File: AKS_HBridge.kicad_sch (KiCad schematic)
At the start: 0 parts

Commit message: schematic brainstorming
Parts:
- added U1: DRV8262DDVR, DDV0044E-IPC_A, symbol custom_components:DRV8262DDVR

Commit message: linux wtf
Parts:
- added C1: 1uF, Capacitor_SMD:C_0603_1608Metric, symbol Device:C_Small
- added NT1: STARGND, symbol Device:NetTie_2
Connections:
- net GND: now also U1.10 (PGND34), U1.13 (PGND12), U1.20 (PGND12), U1.3 (PGND34), NT1.1
- net GNDS: now reaches U1.1 (GND)
- net GNDS: now also U1.44 (GND), NT1.2
- net VBUS: now reaches U1.11 (VM)
- net VBUS: now also U1.12 (VM), U1.2 (VM), U1.21 (VM), C1.1
- net MOT_B: now reaches U1.14 (OUT2)
- net MOT_B: now also U1.15 (OUT2), U1.16 (OUT2), U1.7 (OUT4), U1.8 (OUT4), U1.9 (OUT4)
- net MOT_A: now reaches U1.17 (OUT1)
- net MOT_A: now also U1.18 (OUT1), U1.19 (OUT1), U1.4 (OUT3), U1.5 (OUT3), U1.6 (OUT3)
- net at U1.22 (VCP): now also C1.2
- net VCC: now reaches U1.42 (VCC)
- net VCC: now also U1.43 (DVDD)
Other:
- company: (none) -> iRobotics
- title: (none) -> AKS Brake Actuator H-Bridge
- moved on the sheet: U1

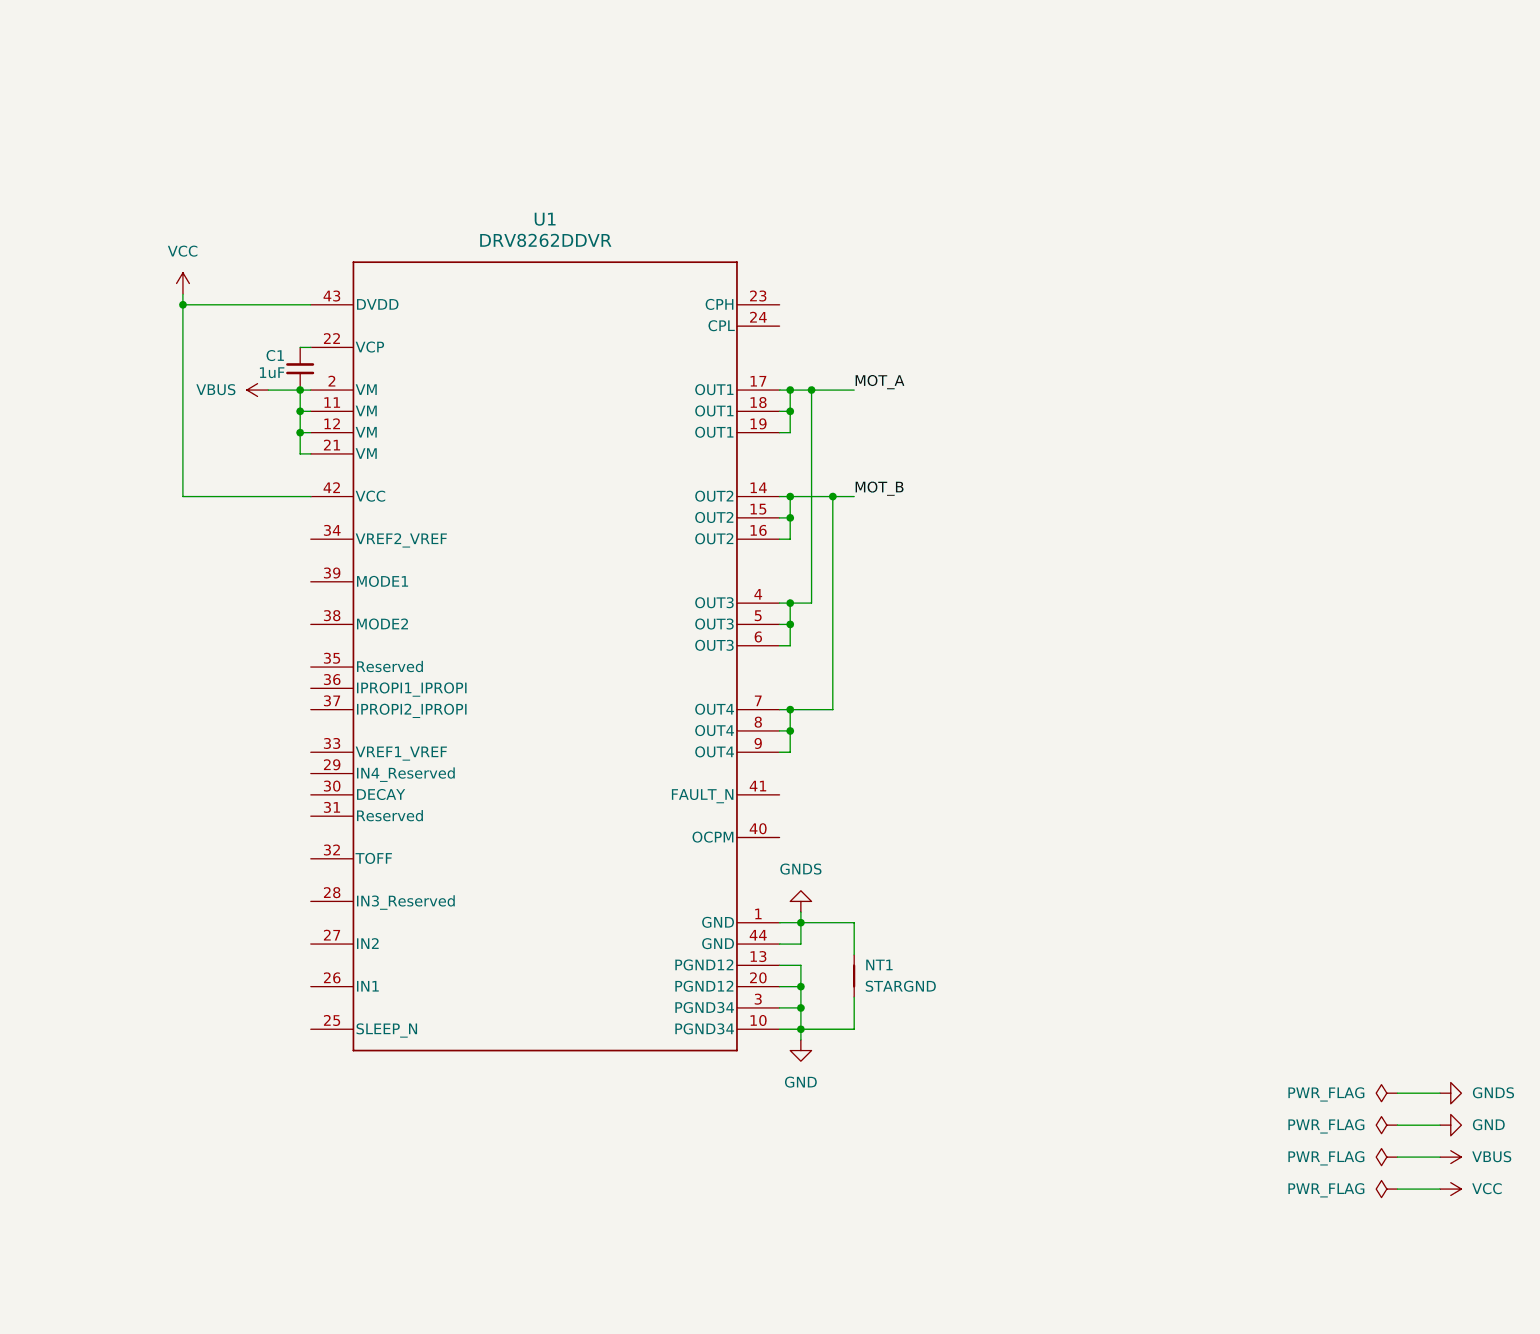
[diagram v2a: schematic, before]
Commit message: schematic done with exception of control connector socket type, probably JST-PH
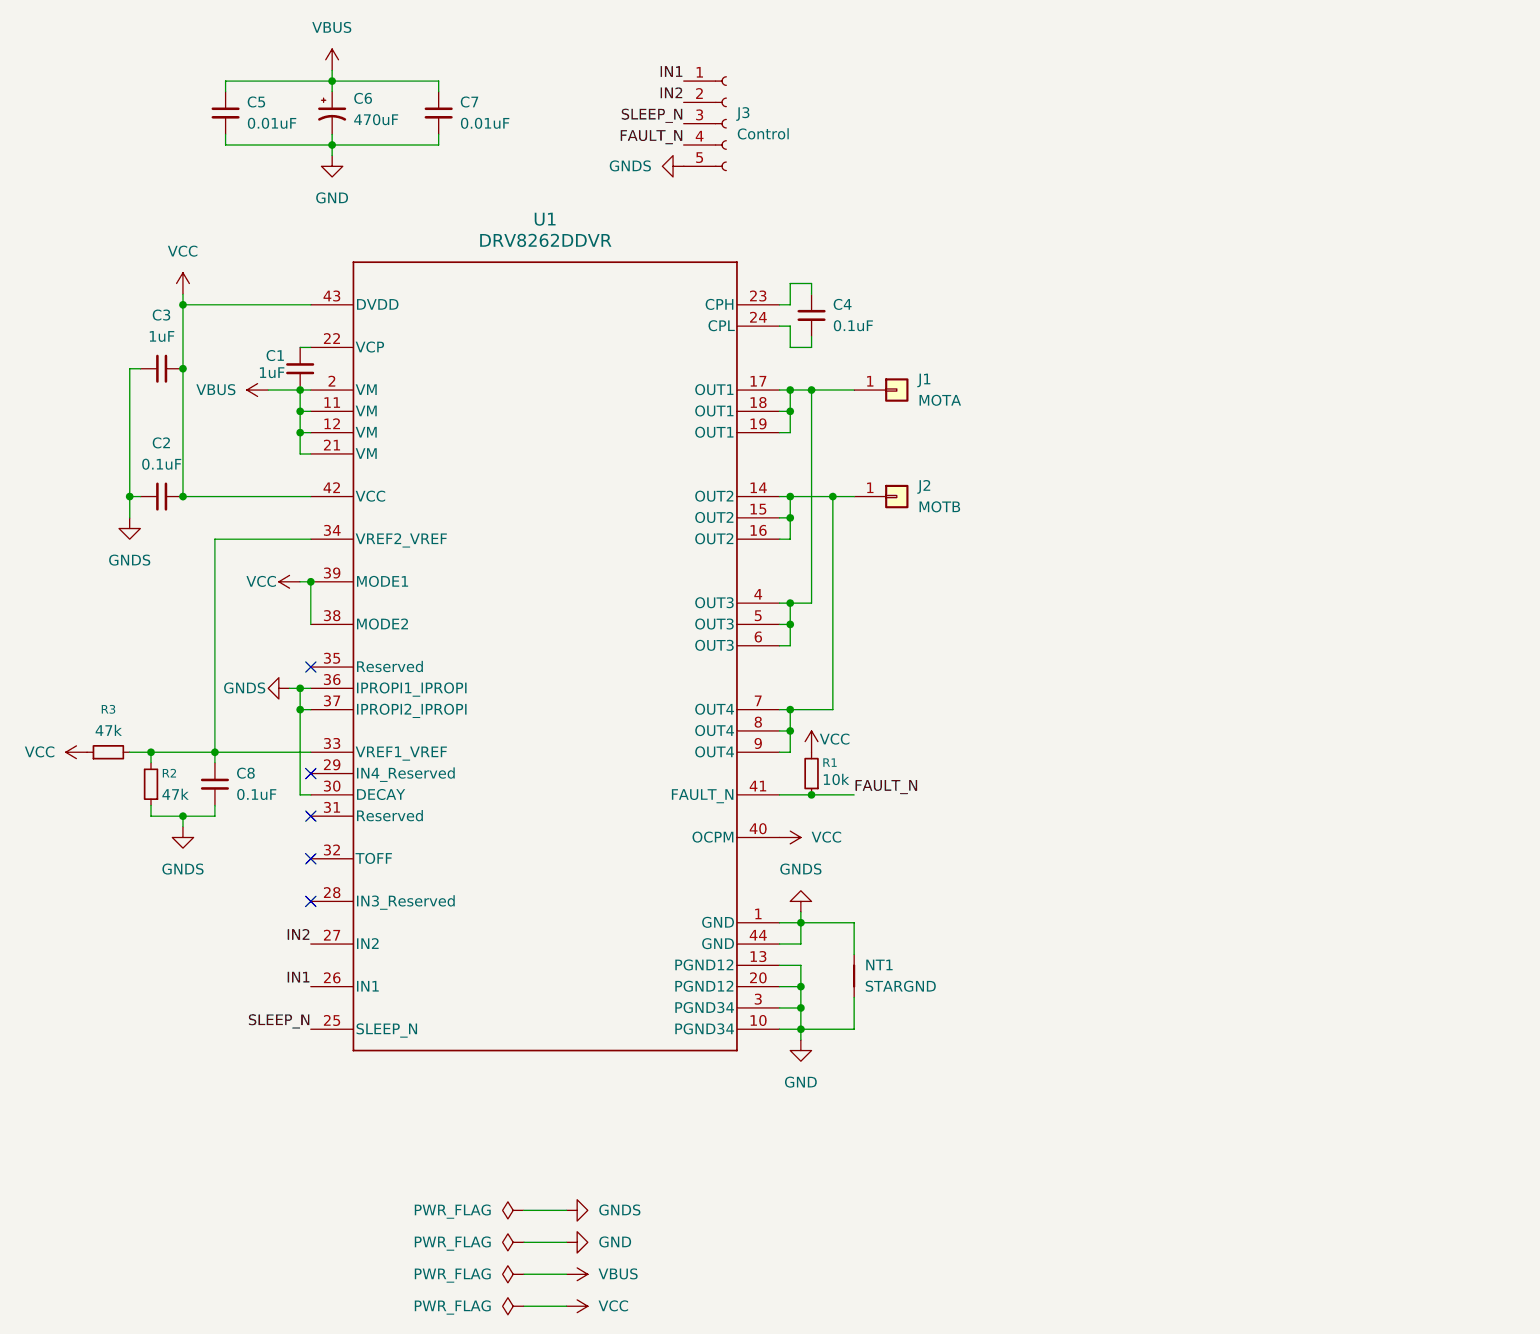
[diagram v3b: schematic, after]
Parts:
- added C2, C8: 0.1uF, Capacitor_SMD:C_0402_1005Metric, symbol Device:C_Small
- added C3: 1uF, Capacitor_SMD:C_0402_1005Metric, symbol Device:C_Small
- added C4: 0.1uF, Capacitor_SMD:C_0603_1608Metric, symbol Device:C_Small
- added C5, C7: 0.01uF, Capacitor_SMD:C_0603_1608Metric, symbol Device:C_Small
- added C6: 470uF, Capacitor_THT:CP_Radial_D16.0mm_P7.50mm, symbol Device:C_Polarized_Small_US
- added J1: MOTA, Connector_Wire:SolderWirePad_1x01_SMD_5x10mm, symbol Connector_Generic:Conn_01x01
- added J2: MOTB, Connector_Wire:SolderWirePad_1x01_SMD_5x10mm, symbol Connector_Generic:Conn_01x01
- added J3: Control, symbol Connector:Conn_01x05_Socket
- added R1: 10k, Resistor_SMD:R_0402_1005Metric, symbol Device:R_Small
- added R2, R3: 47k, Resistor_SMD:R_0402_1005Metric, symbol Device:R_Small
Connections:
- net GND: now also C5.2, C6.2, C7.2
- net GNDS: now also U1.30 (DECAY), U1.36 (IPROPI1_IPROPI), U1.37 (IPROPI2_IPROPI), C2.1, C3.1, C8.2, J3.5 (Pin_5), R2.1
- net VBUS: now also C5.1, C6.1, C7.1
- net VCC: now also U1.38 (MODE2), U1.39 (MODE1), U1.40 (OCPM), C2.2, C3.2, R1.2, R3.1
- net at U1.23 (CPH): now also C4.1
- net at U1.24 (CPL): now also C4.2
- net SLEEP_N: now reaches U1.25 (SLEEP_N)
- net SLEEP_N: now also J3.3 (Pin_3)
- net IN1: now reaches U1.26 (IN1)
- net IN1: now also J3.1 (Pin_1)
- net IN2: now reaches U1.27 (IN2)
- net IN2: now also J3.2 (Pin_2)
- net at U1.33 (VREF1_VREF): now also U1.34 (VREF2_VREF), C8.1, R2.2, R3.2
- net FAULT_N: now reaches U1.41 (FAULT_N)
- net FAULT_N: now also J3.4 (Pin_4), R1.1
- net MOT_A: no longer names the net of U1.17 (OUT1), U1.18 (OUT1), U1.19 (OUT1), U1.4 (OUT3), U1.5 (OUT3), U1.6 (OUT3)
- net MOT_A: now also J1.1 (Pin_1)
- net MOT_B: no longer names the net of U1.14 (OUT2), U1.15 (OUT2), U1.16 (OUT2), U1.7 (OUT4), U1.8 (OUT4), U1.9 (OUT4)
- net MOT_B: now also J2.1 (Pin_1)
- no-connect marks 0 -> 5

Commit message: found control connector footprint
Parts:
- J3: footprint (none) -> Connector_JST:JST_PH_B5B-PH-K_1x05_P2.00mm_Vertical
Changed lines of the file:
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@@
 			)
 		)
-		(property "Footprint" ""
+		(property "Footprint" "Connector_JST:JST_PH_B5B-PH-K_1x05_P2.00mm_Vertical"
 			(at 165.1 33.02 0)
 			(hide yes)

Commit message: pcb layout planning
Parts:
- NT1: footprint (none) -> NetTie:NetTie-2_SMD_Pad2.0mm
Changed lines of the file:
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@@
 			)
 		)
-		(property "Footprint" ""
+		(property "Footprint" "NetTie:NetTie-2_SMD_Pad2.0mm"
 			(at 180.34 134.62 0)
 			(hide yes)

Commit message: more layout and brought in refernce design
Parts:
- added J4: BATT+, Connector_Wire:SolderWirePad_1x01_SMD_5x10mm, symbol Connector_Generic:Conn_01x01
- added J5: BATT-, Connector_Wire:SolderWirePad_1x01_SMD_5x10mm, symbol Connector_Generic:Conn_01x01
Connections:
- net GND: now also J5.1 (Pin_1)
- net VBUS: now also J4.1 (Pin_1)
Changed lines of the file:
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@@
 	)
 	(junction
+		(at 105.41 27.94)
+		(diameter 0)
+		(color 0 0 0 0)
+	)
+	(junction
 		(at 114.3 100.33)
 		(diameter 0)
@@
 	)
 	(junction
+		(at 105.41 35.56)
+		(diameter 0)
+		(color 0 0 0 0)
+	)
+	(junction
 		(at 172.72 92.71)
 		(diameter 0)
@@
 	)
 	(symbol
+		(lib_id "Connector_Generic:Conn_01x01")
+		(at 105.41 40.64 270)
+		(unit 1)
+		(body_style 1)
+		(exclude_from_sim no)
+		(in_bom yes)
+		(on_board yes)
+		(in_pos_files yes)
+		(dnp no)
+		(fields_autoplaced yes)
+		(property "Reference" "J5"
+			(at 107.95 39.3699 90)
+			(show_name no)
+			(do_not_autoplace no)
+			(effects
+				(font
+					(size 1.27 1.27)
+				)
+				(justify left)
+			)
+		)
+		(property "Value" "BATT-"
+			(at 107.95 41.9099 90)
+			(show_name no)
+			(do_not_autoplace no)
+			(effects
+				(font
+					(size 1.27 1.27)
+				)
+				(justify left)
+			)
+		)
+		(property "Footprint" "Connector_Wire:SolderWirePad_1x01_SMD_5x10mm"
+			(at 105.41 40.64 0)
+			(hide yes)
+			(show_name no)
+			(do_not_autoplace no)
+			(effects
+				(font
+					(size 1.27 1.27)
+				)
+			)
+		)
+		(property "Datasheet" ""
+			(at 105.41 40.64 0)
+			(hide yes)
+			(show_name no)
+			(do_not_autoplace no)
+			(effects
+				(font
+					(size 1.27 1.27)
+				)
+			)
+		)
+		(property "Description" "Generic connector, single row, 01x01, script generated (kicad-library-utils/schlib/autogen/connector/)"
+			(at 105.41 40.64 0)
+			(hide yes)
+			(show_name no)
+			(do_not_autoplace no)
+			(effects
+				(font
+					(size 1.27 1.27)
+				)
+			)
+		)
+		(pin "1"
+		)
+		(instances
+			(project "AKS_HBridge"
+				(path "/724ac156-55a4-4fba-8a20-6a27287ebea5"
+					(reference "J5")
+					(unit 1)
+				)
+			)
+		)
+	)
+	(symbol
 		(lib_id "power:PWR_FLAG")
 		(at 140.97 166.37 90)
@@
 					(unit 1)
 				)
+			)
+		)
+	)
+	(symbol
+		(lib_id "Connector_Generic:Conn_01x01")
+		(at 105.41 22.86 90)
+		(unit 1)
+		(body_style 1)
+		(exclude_from_sim no)
+		(in_bom yes)
+		(on_board yes)
+		(in_pos_files yes)
+		(dnp no)
+		(fields_autoplaced yes)
+		(property "Reference" "J4"
+			(at 107.95 21.5899 90)
+			(show_name no)
+			(do_not_autoplace no)
+			(effects
+				(font
+					(size 1.27 1.27)
+				)
+				(justify right)
+			)
+		)
+		(property "Value" "BATT+"
+			(at 107.95 24.1299 90)
+			(show_name no)
+			(do_not_autoplace no)
+			(effects
+				(font
+					(size 1.27 1.27)
+				)
+				(justify right)
+			)
+		)
+		(property "Footprint" "Connector_Wire:SolderWirePad_1x01_SMD_5x10mm"
+			(at 105.41 22.86 0)
+			(hide yes)
+			(show_name no)
+			(do_not_autoplace no)
+			(effects
+				(font
+					(size 1.27 1.27)
+				)
+			)
+		)
+		(property "Datasheet" ""
+			(at 105.41 22.86 0)
+			(hide yes)
+			(show_name no)
+			(do_not_autoplace no)
+			(effects
+				(font
+					(size 1.27 1.27)
+				)
+			)
+		)
+		(property "Description" "Generic connector, single row, 01x01, script generated (kicad-library-utils/schlib/autogen/connector/)"
+			(at 105.41 22.86 0)
+			(hide yes)
+			(show_name no)
+			(do_not_autoplace no)
+			(effects
+				(font
+					(size 1.27 1.27)
+				)
+			)
+		)
+		(pin "1"
+		)
+		(instances
+			(project "AKS_HBridge"
+				(path "/724ac156-55a4-4fba-8a20-6a27287ebea5"
+					(reference "J4")
+					(unit 1)
+				)
